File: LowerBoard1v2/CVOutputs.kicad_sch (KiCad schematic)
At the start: 146 parts, among them U301 DAC7578xPW, U302 TL074, U303 TL074, U304 TL074, U305 TL074, U306 TMUX4051, U307 TL074, U308 TMUX4051, U309 TL074, U310 TL074, U311 TL074, U312 TL074, U313 TMUX4051, U314 TMUX4051, U315 TL074, U316 TL074, U317 TL074, U318 TL074, U319 TL074, U320 TL074, U321 TMUX4051, U322 TMUX4051, U323 TMUX4051

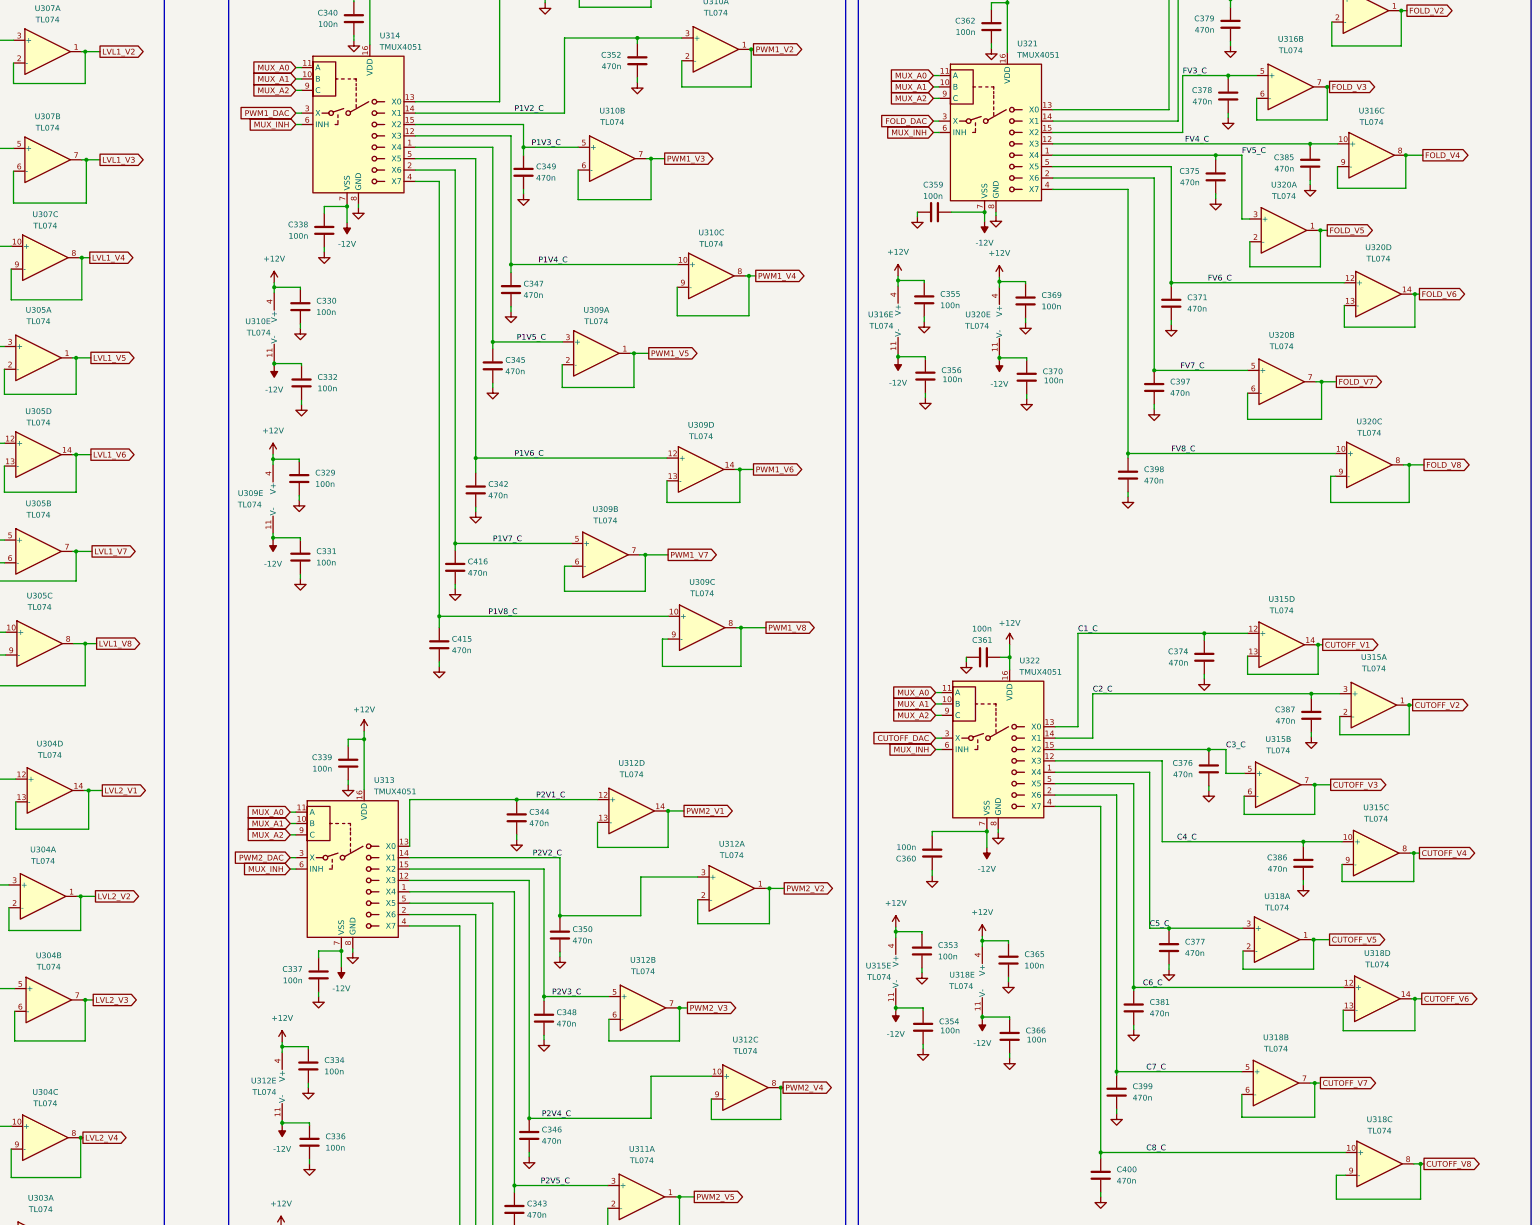
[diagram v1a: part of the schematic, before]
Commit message: all CVs routed wooo
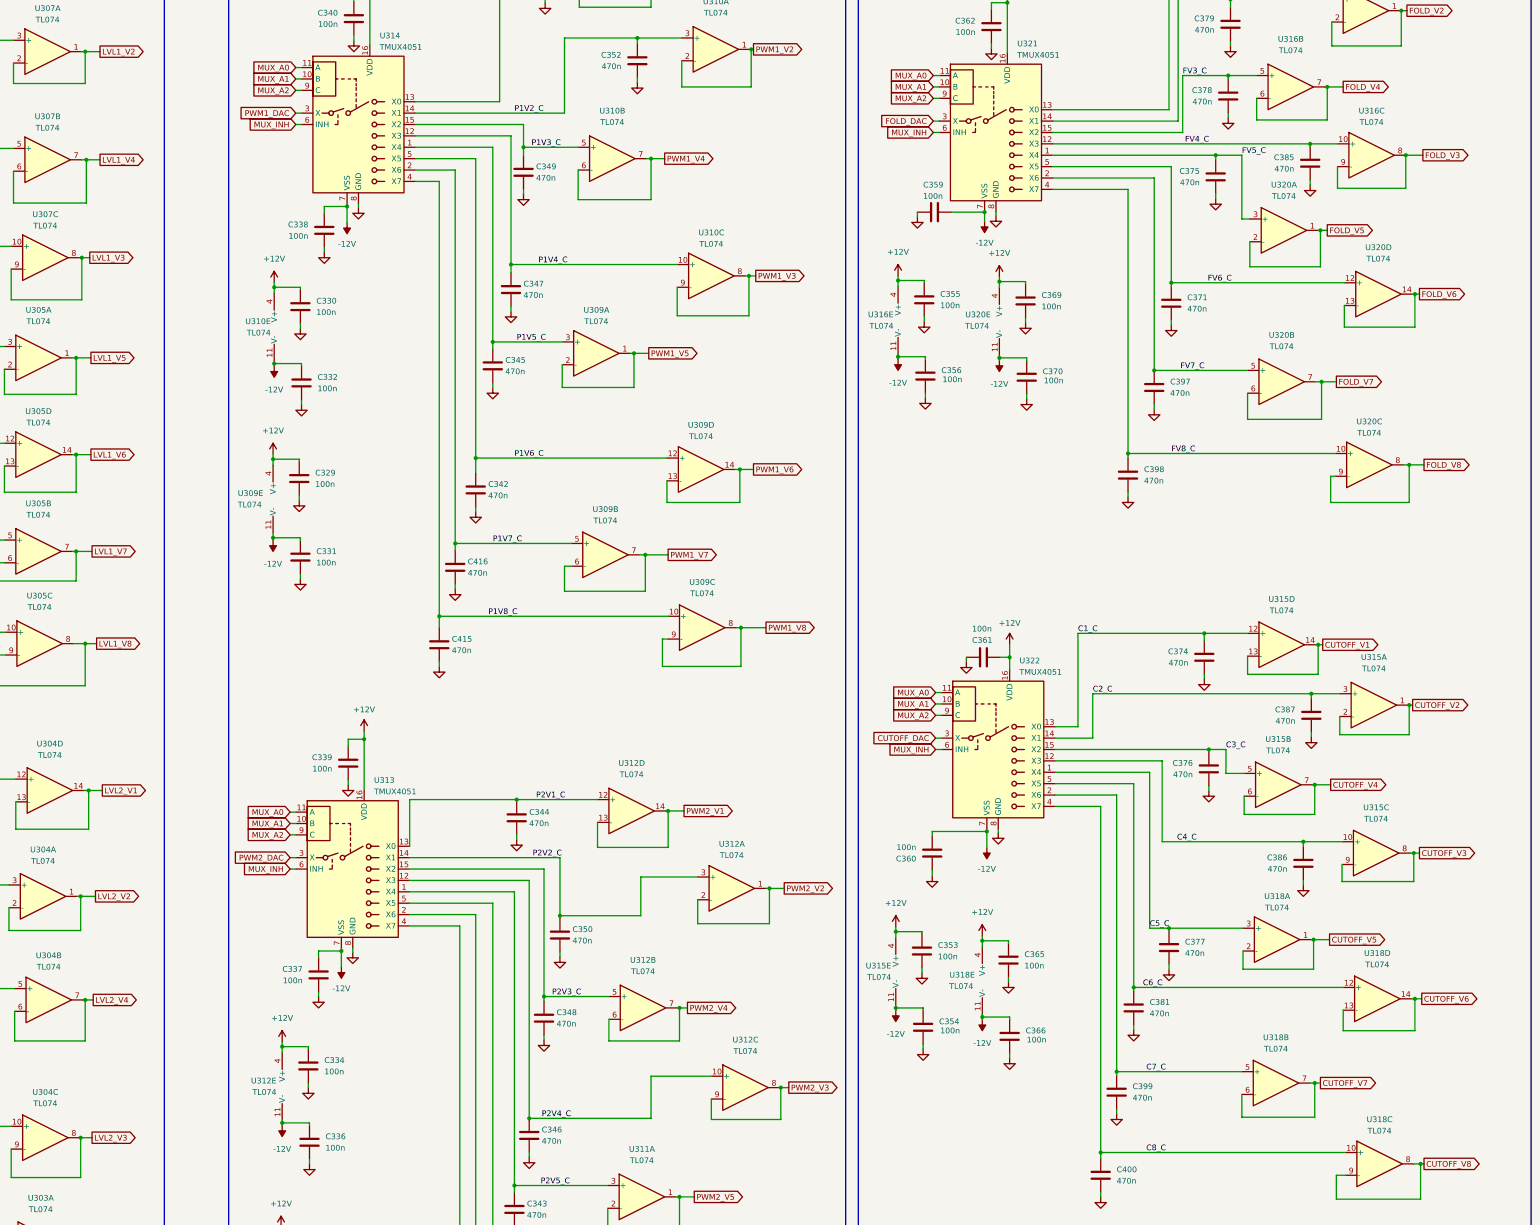
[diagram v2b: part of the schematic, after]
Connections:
- net CUTOFF_V3: now also U315.8, U315.9 (-); no longer U315.6 (-), U315.7
- net CUTOFF_V4: now also U315.6 (-), U315.7; no longer U315.8, U315.9 (-)
- net FOLD_V3: now also U316.8, U316.9 (-); no longer U316.6 (-), U316.7
- net FOLD_V4: now also U316.6 (-), U316.7; no longer U316.8, U316.9 (-)
- net LVL1_V3: now also U307.8, U307.9 (-); no longer U307.6 (-), U307.7
- net LVL1_V4: now also U307.6 (-), U307.7; no longer U307.8, U307.9 (-)
- net LVL2_V3: now also U304.8, U304.9 (-); no longer U304.6 (-), U304.7
- net LVL2_V4: now also U304.6 (-), U304.7; no longer U304.8, U304.9 (-)
- net PWM1_V3: now also U310.8, U310.9 (-); no longer U310.6 (-), U310.7
- net PWM1_V4: now also U310.6 (-), U310.7; no longer U310.8, U310.9 (-)
- net PWM2_V3: now also U312.8, U312.9 (-); no longer U312.6 (-), U312.7
- net PWM2_V4: now also U312.6 (-), U312.7; no longer U312.8, U312.9 (-)
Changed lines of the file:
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@@
 	(wire
 		(pts
-			(xy 586.74 74.676) (xy 587.248 74.676)
+			(xy 586.74 74.676) (xy 590.296 74.676)
 		)
 		(stroke
@@
 	(wire
 		(pts
-			(xy 464.82 297.942) (xy 465.328 297.942)
+			(xy 464.82 297.942) (xy 466.598 297.942)
 		)
 		(stroke
@@
 	(wire
 		(pts
-			(xy 308.61 309.118) (xy 309.118 309.118)
+			(xy 308.61 309.118) (xy 311.15 309.118)
 		)
 		(stroke
@@
 	(global_label "PWM2_V3"
 		(shape output)
-		(at 443.992 280.162 0)
+		(at 466.598 297.942 0)
 		(fields_autoplaced yes)
 		(effects
@@
 		)
 		(property "Intersheetrefs" "${INTERSHEET_REFS}"
-			(at 455.6252 280.162 0)
+			(at 478.2312 297.942 0)
 			(effects
 				(font
@@
 	(global_label "PWM1_V4"
 		(shape output)
-		(at 459.232 116.84 0)
+		(at 438.912 90.678 0)
 		(fields_autoplaced yes)
 		(effects
@@
 		)
 		(property "Intersheetrefs" "${INTERSHEET_REFS}"
-			(at 470.8652 116.84 0)
+			(at 450.5452 90.678 0)
 			(effects
 				(font
@@
 	(global_label "LVL1_V3"
 		(shape output)
-		(at 312.928 90.932 0)
+		(at 310.642 112.776 0)
 		(fields_autoplaced yes)
 		(effects
@@
 		)
 		(property "Intersheetrefs" "${INTERSHEET_REFS}"
-			(at 323.5332 90.932 0)
+			(at 321.2472 112.776 0)
 			(effects
 				(font
@@
 	(global_label "PWM1_V3"
 		(shape output)
-		(at 438.912 90.678 0)
+		(at 459.232 116.84 0)
 		(fields_autoplaced yes)
 		(effects
@@
 		)
 		(property "Intersheetrefs" "${INTERSHEET_REFS}"
-			(at 450.5452 90.678 0)
+			(at 470.8652 116.84 0)
 			(effects
 				(font
@@
 	(global_label "FOLD_V3"
 		(shape output)
-		(at 587.248 74.676 0)
+		(at 608.076 89.916 0)
 		(fields_autoplaced yes)
 		(effects
@@
 		)
 		(property "Intersheetrefs" "${INTERSHEET_REFS}"
-			(at 598.2161 74.676 0)
+			(at 619.0441 89.916 0)
 			(effects
 				(font
@@
 	(global_label "CUTOFF_V3"
 		(shape output)
-		(at 587.502 230.378 0)
+		(at 607.314 245.618 0)
 		(fields_autoplaced yes)
 		(effects
@@
 		)
 		(property "Intersheetrefs" "${INTERSHEET_REFS}"
-			(at 600.8287 230.378 0)
+			(at 620.6407 245.618 0)
 			(effects
 				(font
@@
 	(global_label "CUTOFF_V4"
 		(shape output)
-		(at 607.314 245.618 0)
+		(at 587.502 230.378 0)
 		(fields_autoplaced yes)
 		(effects
@@
 		)
 		(property "Intersheetrefs" "${INTERSHEET_REFS}"
-			(at 620.6407 245.618 0)
+			(at 600.8287 230.378 0)
 			(effects
 				(font
@@
 	(global_label "LVL2_V3"
 		(shape output)
-		(at 311.404 278.384 0)
+		(at 311.15 309.118 0)
 		(fields_autoplaced yes)
 		(effects
@@
 		)
 		(property "Intersheetrefs" "${INTERSHEET_REFS}"
-			(at 322.0092 278.384 0)
+			(at 321.7552 309.118 0)
 			(effects
 				(font
@@
 	(global_label "LVL2_V4"
 		(shape output)
-		(at 309.118 309.118 0)
+		(at 311.404 278.384 0)
 		(fields_autoplaced yes)
 		(effects
@@
 		)
 		(property "Intersheetrefs" "${INTERSHEET_REFS}"
-			(at 319.7232 309.118 0)
+			(at 322.0092 278.384 0)
 			(effects
 				(font
@@
 	(global_label "FOLD_V4"
 		(shape output)
-		(at 608.076 89.916 0)
+		(at 590.296 74.676 0)
 		(fields_autoplaced yes)
 		(effects
@@
 		)
 		(property "Intersheetrefs" "${INTERSHEET_REFS}"
-			(at 619.0441 89.916 0)
+			(at 601.2641 74.676 0)
 			(effects
 				(font
@@
 	(global_label "PWM2_V4"
 		(shape output)
-		(at 465.328 297.942 0)
+		(at 443.992 280.162 0)
 		(fields_autoplaced yes)
 		(effects
@@
 		)
 		(property "Intersheetrefs" "${INTERSHEET_REFS}"
-			(at 476.9612 297.942 0)
+			(at 455.6252 280.162 0)
 			(effects
 				(font
@@
 	(global_label "LVL1_V4"
 		(shape output)
-		(at 310.642 112.776 0)
+		(at 312.928 90.932 0)
 		(fields_autoplaced yes)
 		(effects
@@
 		)
 		(property "Intersheetrefs" "${INTERSHEET_REFS}"
-			(at 321.2472 112.776 0)
+			(at 323.5332 90.932 0)
 			(effects
 				(font
